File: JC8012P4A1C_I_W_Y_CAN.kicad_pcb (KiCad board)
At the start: 2 copper layers, 66 x 54 mm, 39 parts, among them J1 610110249121, J2 68711414522, J3 653104131822, Q1 Si4948BEY, U1 TLE9250VSJ, U2 171030601

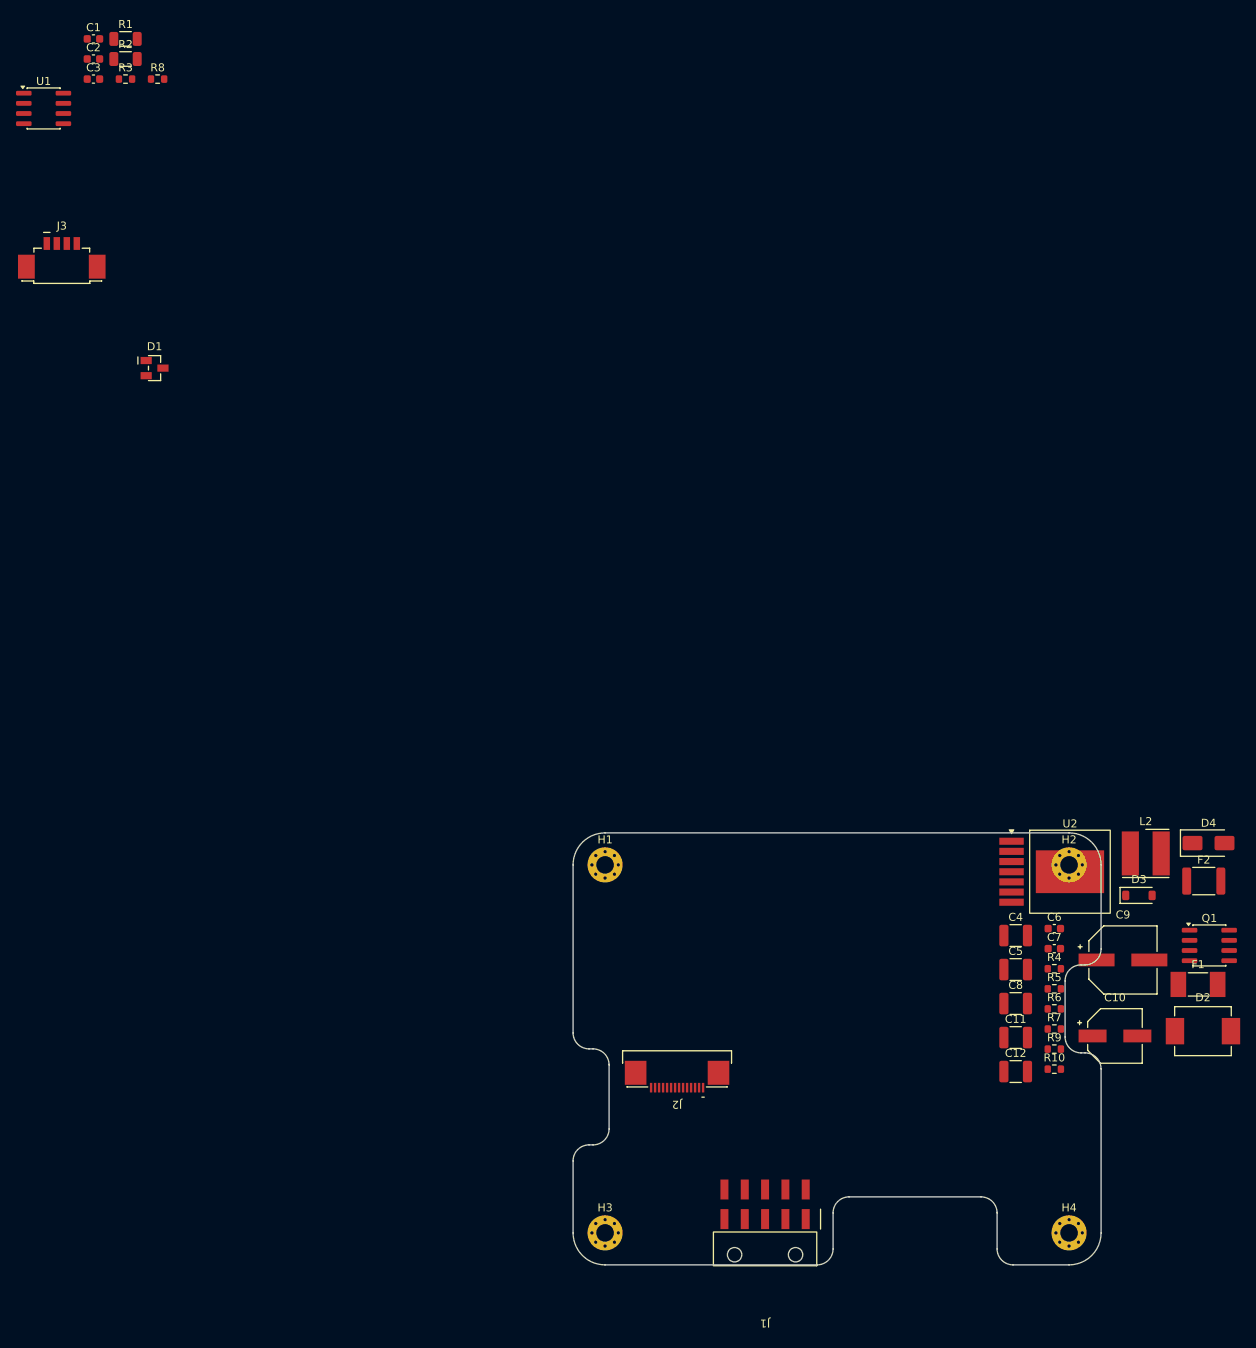
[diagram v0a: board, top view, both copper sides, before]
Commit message: Rough placement, buck converter per datasheet layout recommendation
- CAN part on the left: U1 with C2/C3/R3, split termination R1/R2/C1,
  D1 and R8 next to J1
- U2 placed as in the 171030601 layout recommendation (datasheet
  p. 39-44): pins pointing down, C_IN (C12, C4) vertical left of pin 1,
  C_OUT (C5, C11) vertical right of pin 7, GND pads in one row with the
  PGND pad, small parts in two rows below the pins
  (R5 C6 C7 / R9 R10 R7 R6)
- EMI filter L2/C8 and damping capacitor C9 left of the converter,
  input chain F1 -> D2 -> Q1 (D3, R4) bottom centre, C10 at the output,
  TBC supply D4/F2 top centre, J3 at the right edge towards CN2
- No courtyard overlaps; not routed yet

Co-Authored-By: Claude Opus 5.5 <noreply@anthropic.com>
Claude-Session: https://claude.ai/code/session_014h8cGi8SRWthYdGFH1Qgzz
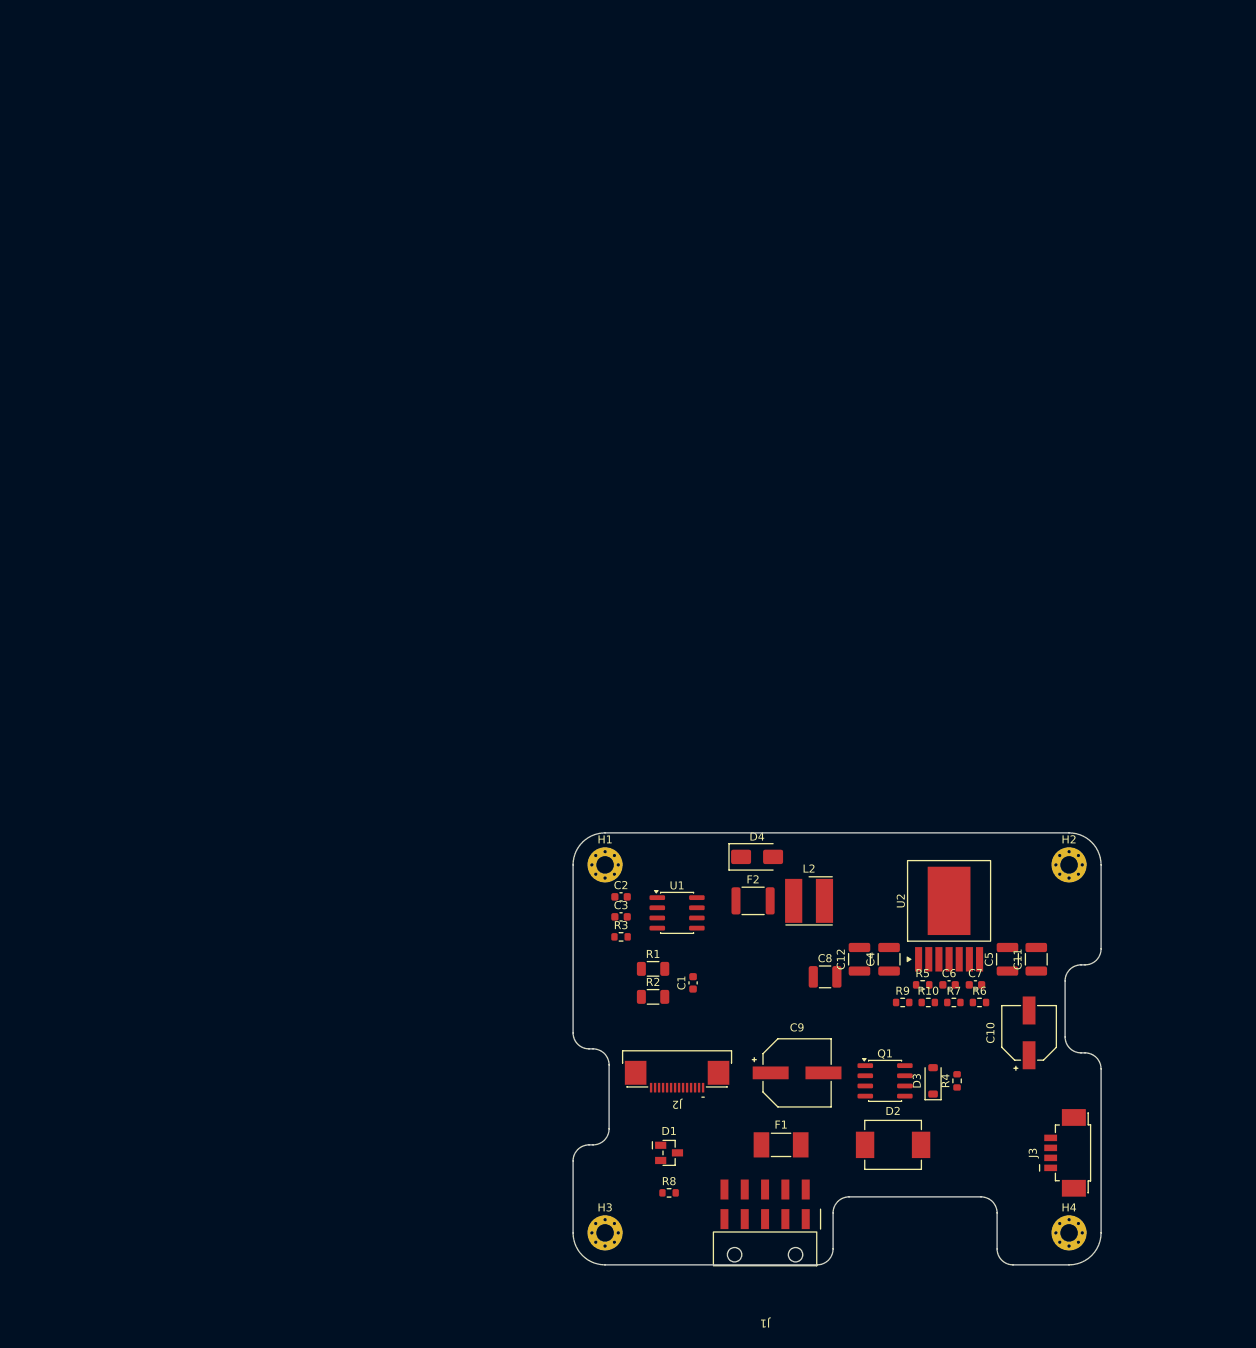
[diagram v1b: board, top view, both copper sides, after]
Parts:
- moved J3 168.1 mm to (162.5, 140.0), turned to 90 degrees
- moved R8 153.2 mm to (112.0, 145.0)
- moved C1 139.8 mm to (115.0, 118.8), turned to 90 degrees
- moved R2 134.5 mm to (110.0, 120.5)
- moved R1 133.6 mm to (110.0, 117.0)
- moved U1 128.0 mm to (113.0, 110.0)
- moved R3 123.8 mm to (106.0, 113.0)
- moved C2 123.8 mm to (106.0, 108.0)
- moved C3 123.8 mm to (106.0, 110.5)
- moved D1 117.3 mm to (112.0, 140.0)
- moved D4 56.5 mm to (123.0, 103.0)
- moved F2 56.4 mm to (122.5, 108.5)
- moved F1 55.8 mm to (126.0, 139.0)
- moved Q1 43.9 mm to (139.0, 131.0)
- moved C9 43.1 mm to (128.0, 130.0)
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
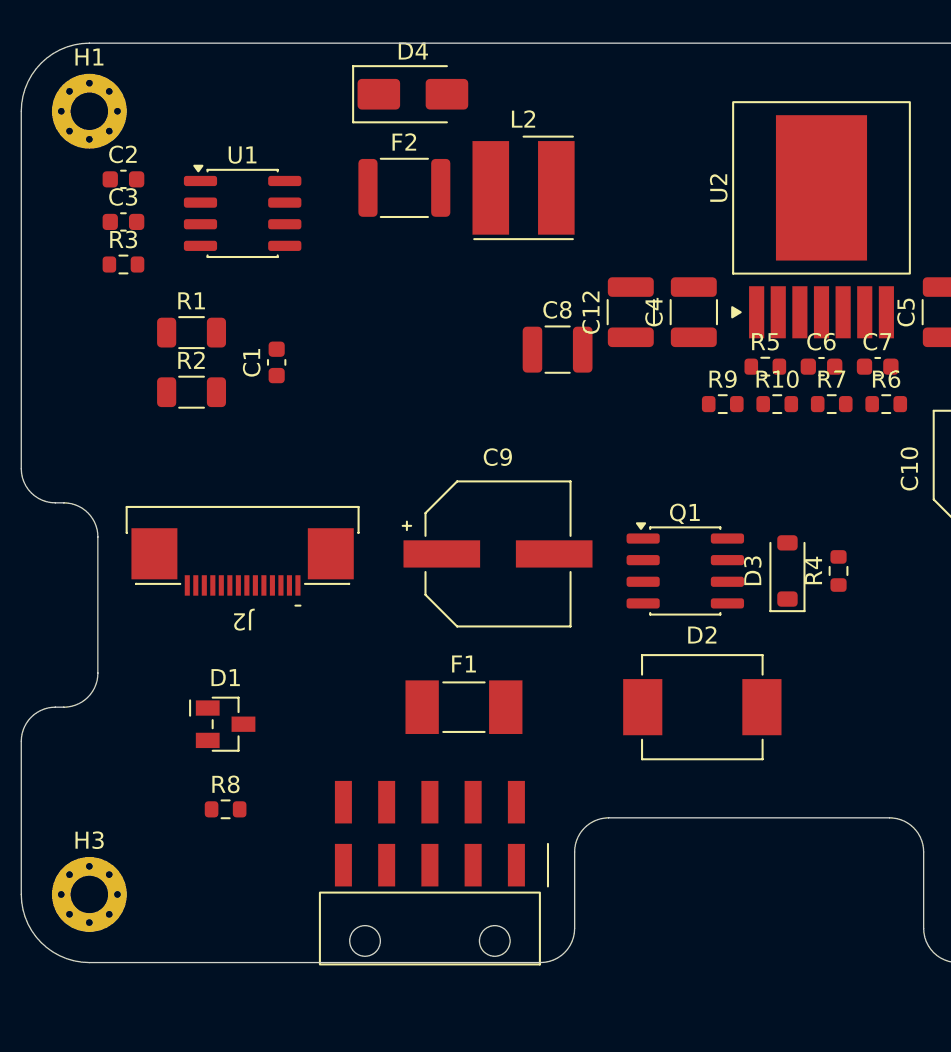
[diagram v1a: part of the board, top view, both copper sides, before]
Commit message: Refined placement (done in KiCad)
- CAN group (U1, C2, C3, R3, R1/R2/C1, D1) between J2 and J1:
  CAN_H/CAN_L ~25 mm instead of ~57 mm, TXD/RXD/NEN 5-12 mm
- F1 directly above J1 pin 8 (ECU_PWR_IN), D2/Q1/D3/R4 next to it
- TBC supply D4/F2 next to Q1 and J1 (TBC_PWR_OUT 15 mm instead of 36)
- C9 (6.5 mm high) moved out of the FFC path above J2
- J2 4.35 mm closer to the top edge
- Buck converter block per datasheet unchanged
- DRC: no courtyard or clearance violations, schematic parity OK

Co-Authored-By: Claude Opus 5.5 <noreply@anthropic.com>
Claude-Session: https://claude.ai/code/session_014h8cGi8SRWthYdGFH1Qgzz
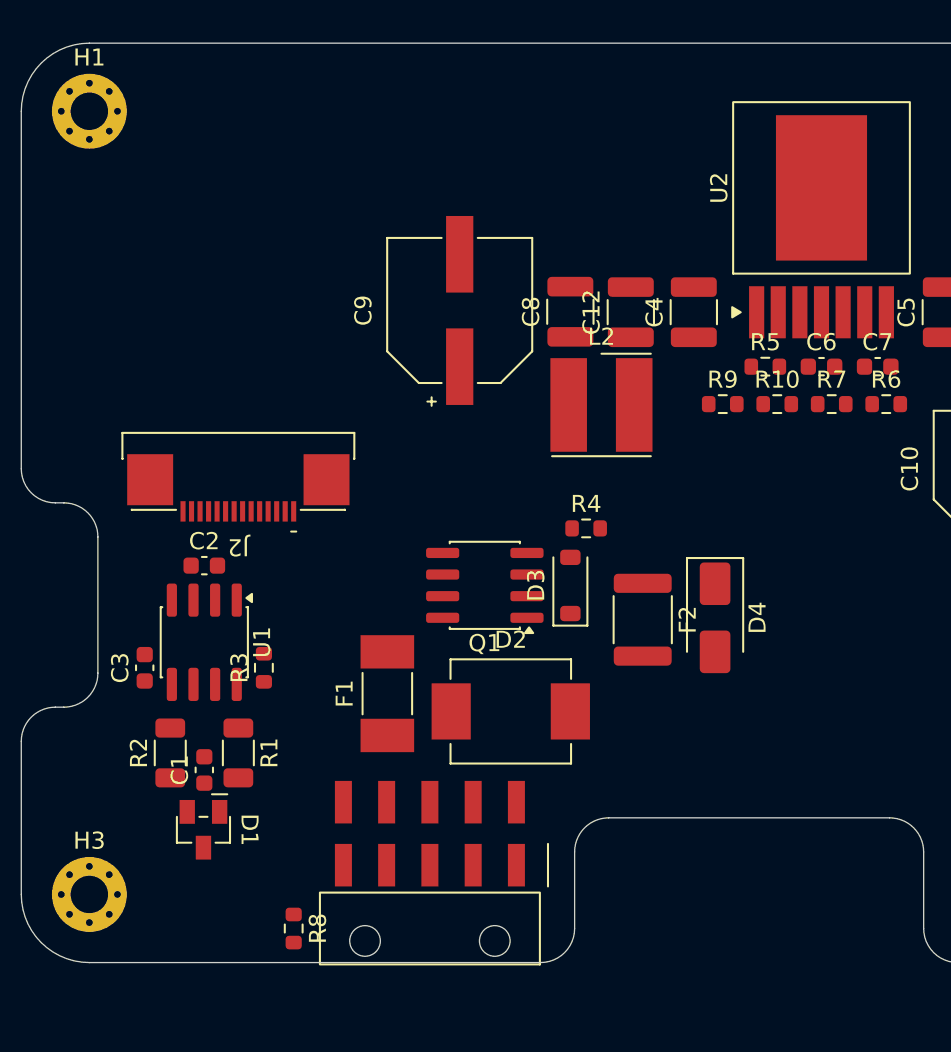
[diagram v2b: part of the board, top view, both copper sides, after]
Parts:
- moved D4 35.5 mm to (140.8, 133.8), turned to -90 degrees
- moved F2 29.0 mm to (136.5, 133.9), turned to -90 degrees
- moved C3 26.2 mm to (107.2, 136.7), turned to 90 degrees
- moved U1 25.3 mm to (110.8, 135.2), turned to -90 degrees
- moved R3 25.1 mm to (114.2, 136.7), turned to 90 degrees
- moved R1 24.8 mm to (112.8, 141.7), turned to -90 degrees
- moved C1 24.3 mm to (110.8, 142.7)
- moved C2 23.2 mm to (110.8, 130.7)
- moved R2 21.2 mm to (108.8, 141.7), turned to 90 degrees
- moved R4 15.0 mm to (133.2, 128.5), turned to 0 degrees
- moved C9 14.5 mm to (125.8, 115.7), turned to 90 degrees
- moved L2 13.5 mm to (134.1, 121.2)
- moved D3 12.8 mm to (132.2, 131.8)
- moved Q1 11.8 mm to (127.2, 131.8), turned to 180 degrees
- moved D2 11.3 mm to (128.8, 139.2)
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
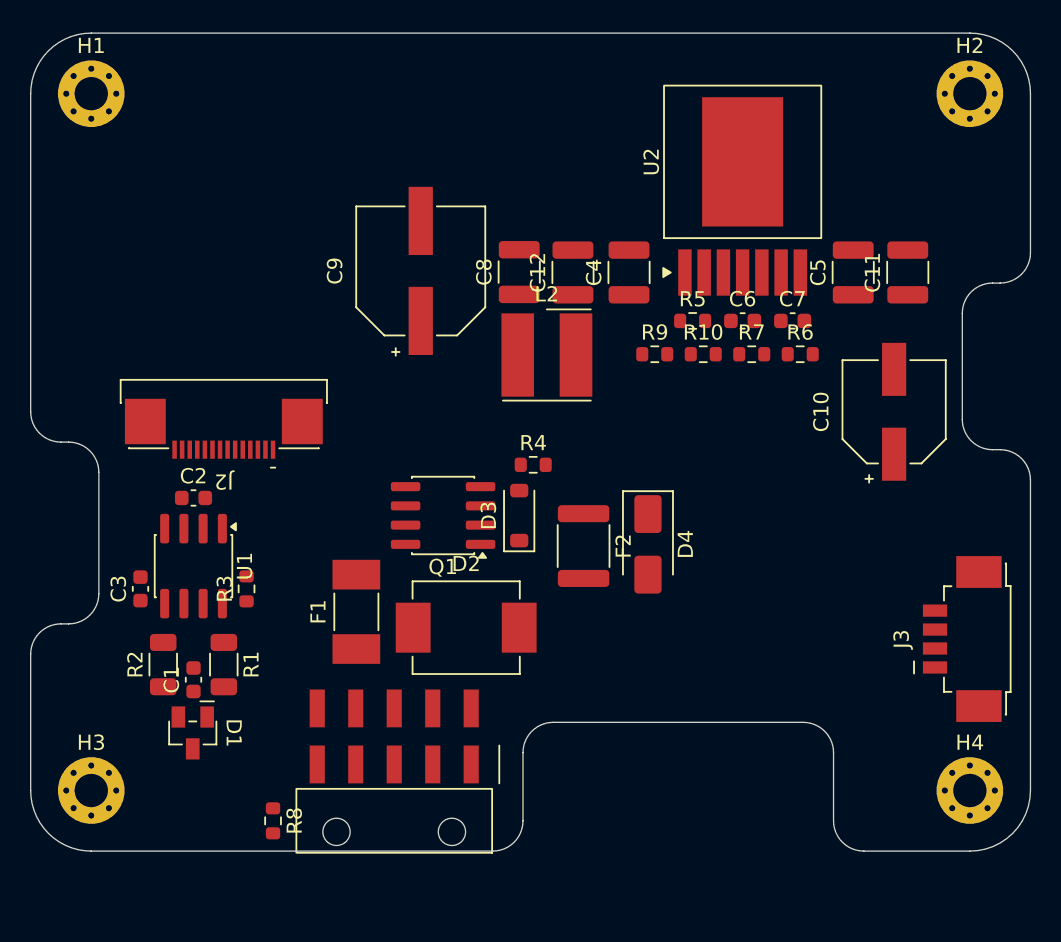
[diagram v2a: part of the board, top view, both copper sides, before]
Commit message: 6-layer stackup, planes, thermal vias under U2, net classes
- 6 copper layers: F.Cu parts/signals, In1 GND, In2 +5V, In3 free for
  signals, In4 GND, B.Cu GND (JLCPCB 6-layer with epoxy filled and
  capped vias, same price as 2-layer with plugged vias)
- GND zones on F.Cu/In1/In4/B.Cu, +5V zone on In2 (filled with
  kicad-cli; +5V plane still isolated until the first +5V vias exist)
- 77 thermal vias 0.45/0.2 mm, 7 x 11 on a 0.75 mm grid under the U2
  exposed pad (171030601 datasheet p. 44: drill <= 250 um, 750 um
  pitch), intended as filled & capped (via-in-pad)
- U2 EP and GND pads of C4/C12/C5/C11 solidly connected to the zones
- Net classes: Power 0.8 mm / 0.25 mm (ECU_PWR_IN, ECU_PWR, VIN_PROT,
  VIN_BUCK, +5V), CAN 0.3 mm / 0.25 mm (CAN_H, CAN_L, CAN_SPLIT),
  Default 0.25 mm / 0.2 mm; all vias 0.45/0.2 mm, min drill 0.2 mm
- Layers, zones and vias created with the KiCAD-MCP-Server

Co-Authored-By: Claude Opus 5.5 <noreply@anthropic.com>
Claude-Session: https://claude.ai/code/session_014h8cGi8SRWthYdGFH1Qgzz
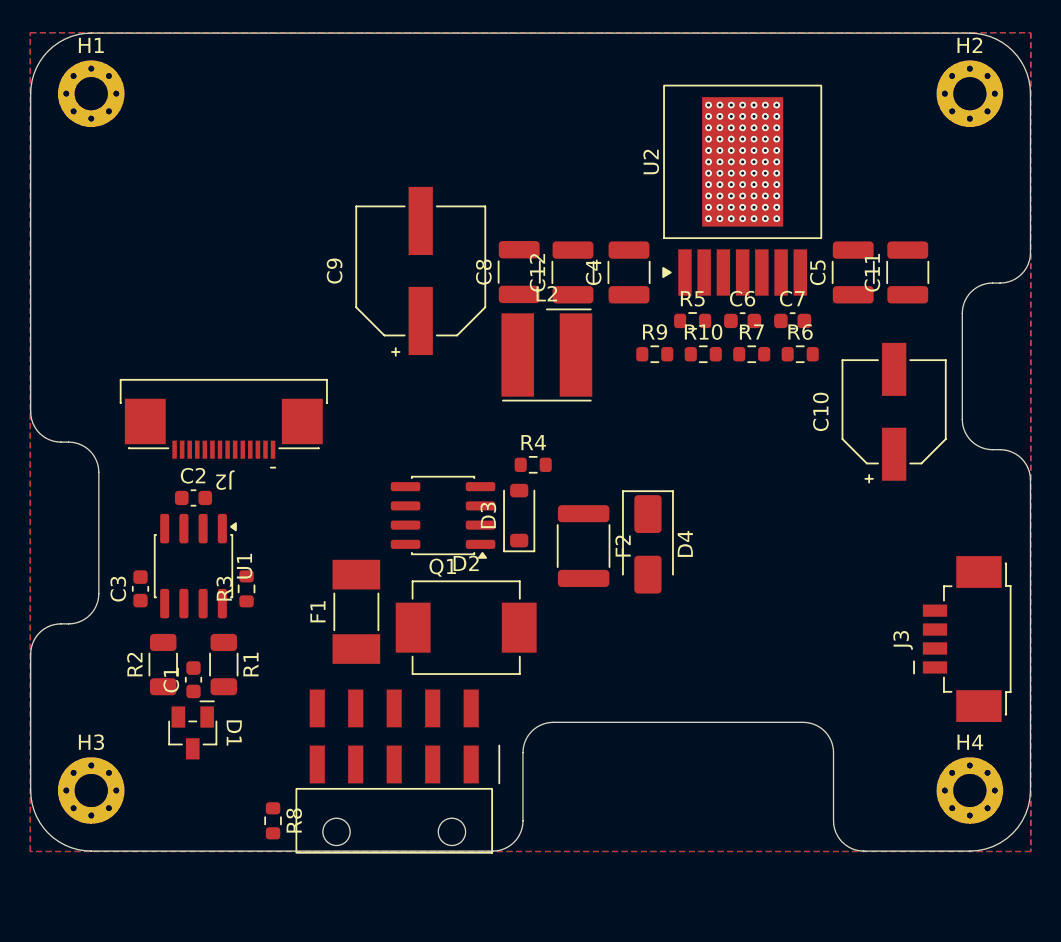
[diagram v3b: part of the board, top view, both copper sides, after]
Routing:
- net GND: vias 0 -> 77
- added copper zone on In2.Cu, net +5V
- added copper zone on B.Cu, net GND
- added copper zone on F.Cu, net GND
- added copper zone on In1.Cu, net GND
- added copper zone on In4.Cu, net GND
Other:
- copper layers 2 -> 6
